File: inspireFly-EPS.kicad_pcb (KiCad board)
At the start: 4 copper layers, 88 x 94.5 mm, 123 parts, among them J1 USB4085-GF-A_REVB, J2 Conn_01x02_Pin, Q1 SQJ123ELP-T1_GE3, Q10 SQJA62EP-T1_GE3, Q3 SQJA62EP-T1_GE3, Q4 SQJA62EP-T1_GE3, Q5 SQJA62EP-T1_GE3, Q6 SQJA62EP-T1_GE3, Q7 SQJA62EP-T1_GE3, Q8 SQJA62EP-T1_GE3, Q9 SQJA62EP-T1_GE3, SW1 SW_Push, SW2 SW_Push, U1 STM32U575RIT6, U2 BQ25750RRVR, U3 TCAN332DCNR, U4 MAX77504AAFC+T, U6 INA180A3IDBVT, U8 TPS63070RNMR, U9 TPS63070RNMR, Y1 Crystal_GND2

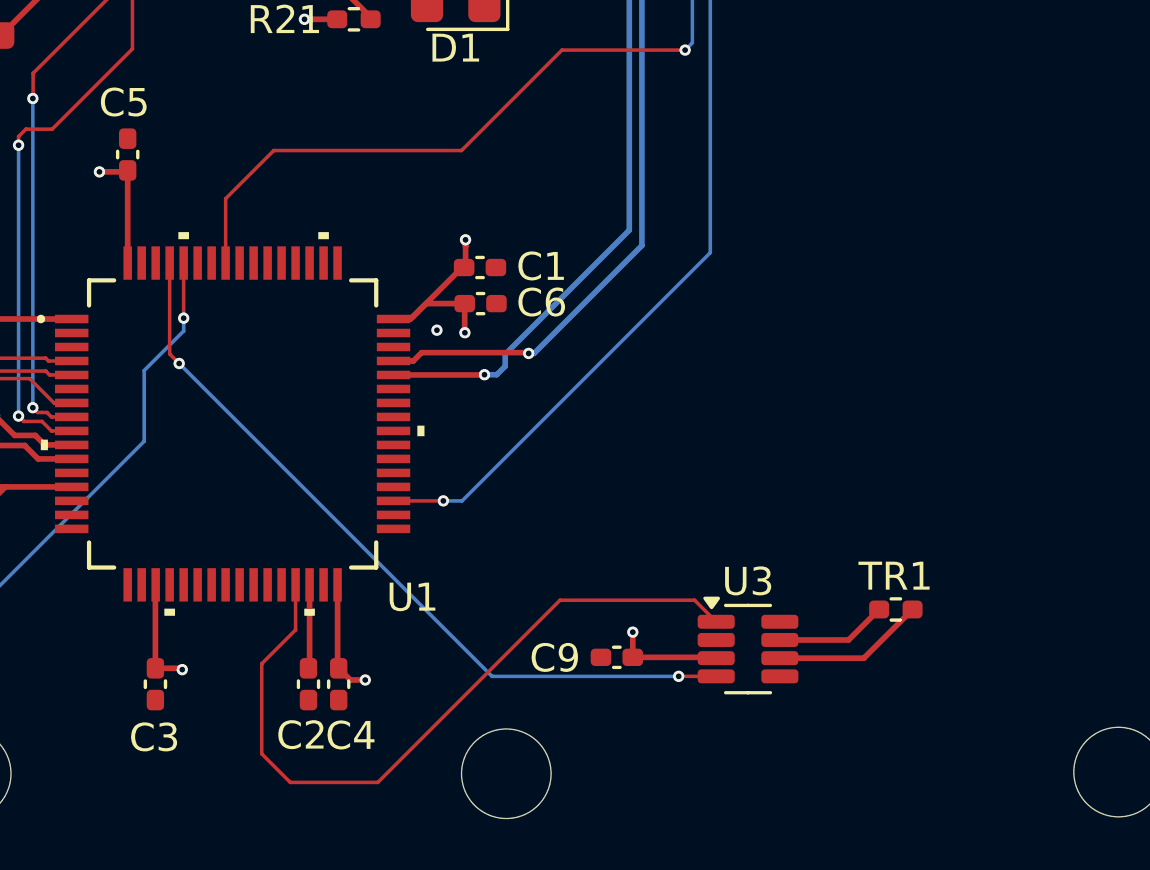
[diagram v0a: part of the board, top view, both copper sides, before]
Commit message: Updated the ST575 to have a 14 pin debugger
Routed and added to schematic.
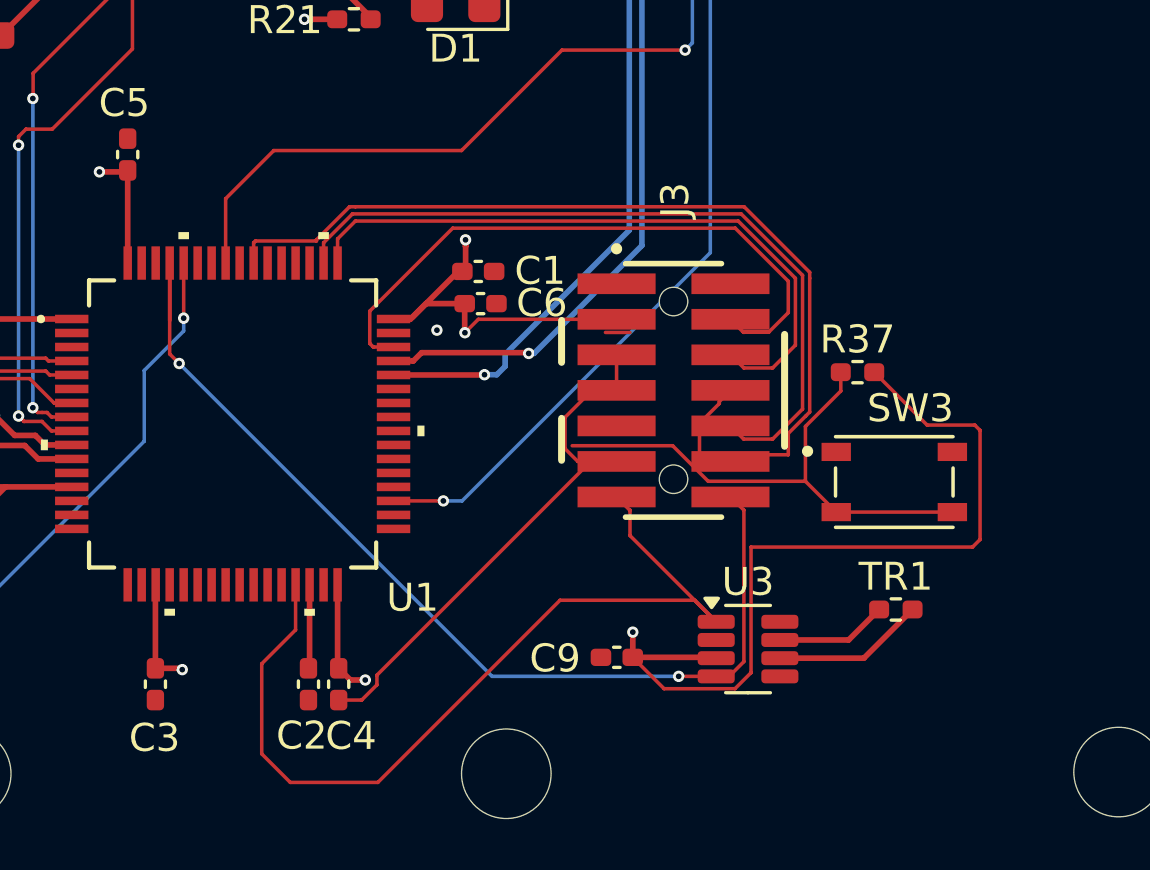
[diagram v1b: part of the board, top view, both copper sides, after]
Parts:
- added J3: FTSH-107-01-L-DV-K-A, inspireFly-EPS-footprints:SAMTEC_FTSH-107-01-L-DV-K-A, F.Cu at (77.0, 89.0)
- added R37: 10K, Resistor_SMD:R_0402_1005Metric_Pad0.72x0.64mm_HandSolder, F.Cu at (83.5, 88.3)
- added SW3: SW_Push, inspireFly-EPS-footprints:SW_PTS810_SJM_250_SMTR_LFS, F.Cu at (84.8, 92.2)
- moved C1 0.15 mm to (70.0, 84.7)
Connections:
- U1 pad 46: unconnected-(U1A-PA13-Pad46) -> JTMS/SWDIO
- U1 pad 49: unconnected-(U1A-PA14-Pad49) -> JTCK/SWCLK
- U1 pad 50: unconnected-(U1A-PA15-Pad50) -> JTDI
- U1 pad 55: unconnected-(U1A-PB3-Pad55) -> SWO
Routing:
- net SWO: track 0.00 -> 34.9 mm
- net +3.3V: track 56.8 -> 89.5 mm
- net JTDI: track 0.00 -> 27.2 mm
- net JTMS/SWDIO: track 0.00 -> 23.6 mm
- net JTCK/SWCLK: track 0.00 -> 23.6 mm
- net GND: track 52.1 -> 72.4 mm
- net NRST: track 0.00 -> 19.0 mm
- net CAN_RX: track 27.6 -> 36.9 mm
- net CAN_TX: track 26.2 -> 32.2 mm

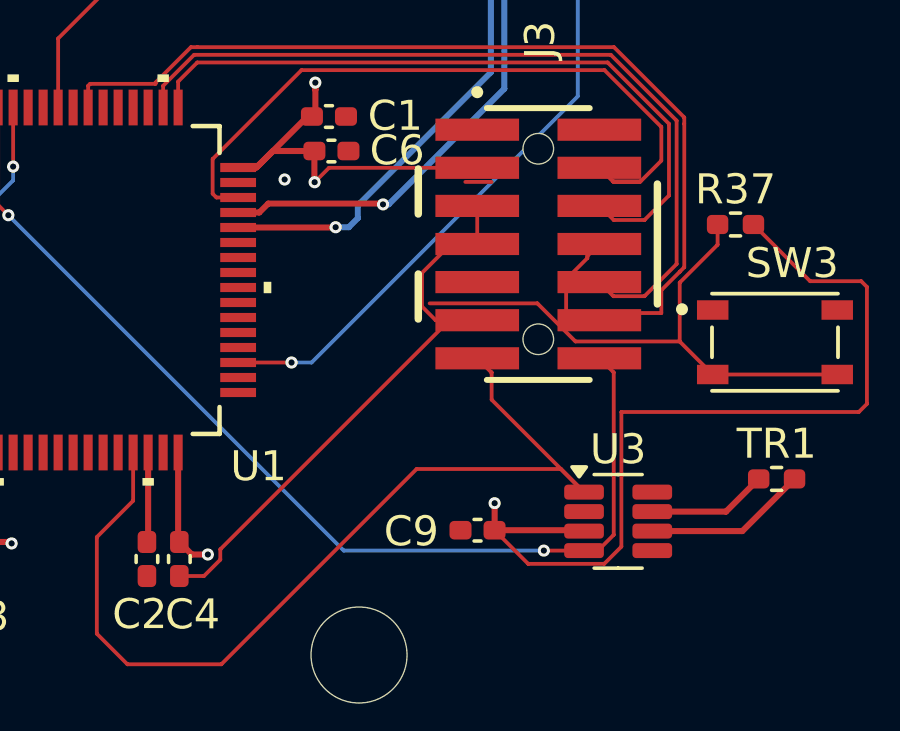
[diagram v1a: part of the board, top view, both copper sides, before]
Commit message: Routing and STLink debugger.
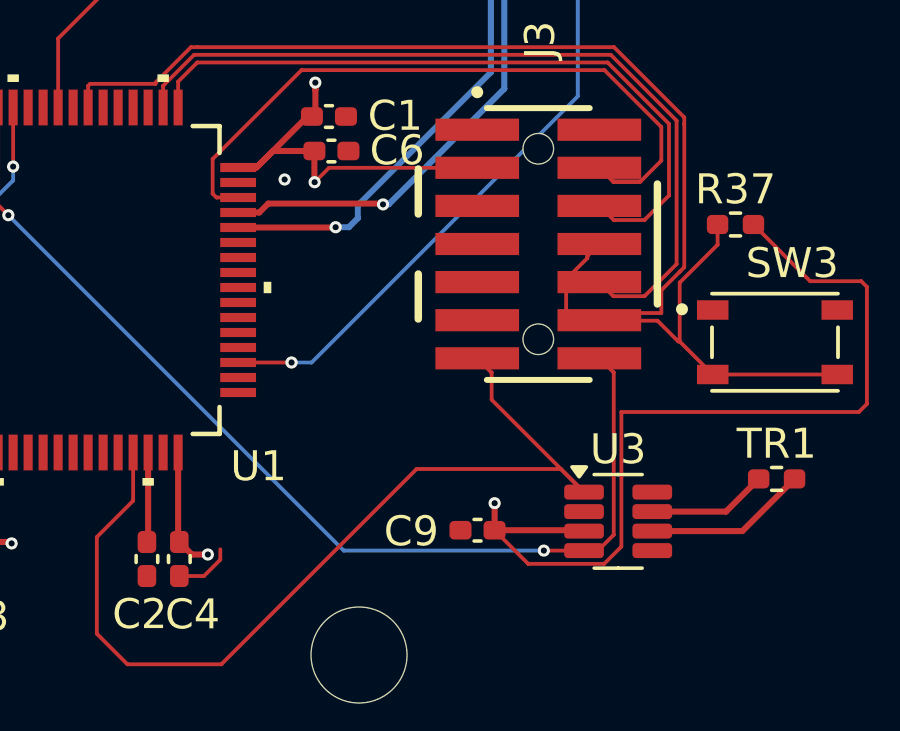
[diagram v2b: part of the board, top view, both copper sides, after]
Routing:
- net GND: track 72.4 -> 55.8 mm
- net NRST: track 19.0 -> 13.1 mm
- net +3.3V: track 89.5 -> 88.7 mm
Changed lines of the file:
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@@
 			(psa4output no)
 			(plot_black_and_white yes)
+			(plotinvisibletext no)
 			(sketchpadsonfab no)
 			(plotpadnumbers no)
@@
 	)
 	(segment
-		(start 74.522 86.88)
-		(end 75.4 86.88)
-		(width 0.127)
-		(layer "F.Cu")
-		(net 1)
-	)
-	(segment
 		(start 102.085063 51.33)
 		(end 101.405 52.010063)
@@
 	)
 	(segment
-		(start 73.534376 91.49)
-		(end 73.0785 91.034124)
-		(width 0.127)
-		(layer "F.Cu")
-		(net 125)
-	)
-	(segment
 		(start 63.749089 66.709811)
 		(end 62.9989 67.46)
@@
 	)
 	(segment
-		(start 73.0785 91.034124)
-		(end 73.0785 89.9135)
-		(width 0.127)
-		(layer "F.Cu")
-		(net 125)
-	)
-	(segment
 		(start 74.92 91.49)
 		(end 73.993745 91.49)
@@
 	)
 	(segment
-		(start 73.0785 89.9135)
-		(end 74.042 88.95)
-		(width 0.127)
-		(layer "F.Cu")
-		(net 125)
-	)
-	(segment
 		(start 88.76 55.73518)
 		(end 89.51 56.48518)
@@
 	)
 	(segment
-		(start 74.92 88.95)
-		(end 74.92 87.68)
-		(width 0.127)
-		(layer "F.Cu")
-		(net 125)
-	)
-	(segment
 		(start 89.51 56.48518)
 		(end 89.22982 56.205)
@@
 	)
 	(segment
-		(start 73.993745 91.49)
-		(end 66.3561 99.127645)
-		(width 0.127)
-		(layer "F.Cu")
-		(net 125)
-	)
-	(segment
 		(start 87.89 45.65)
 		(end 87.89 46.3875)
@@
 	)
 	(segment
-		(start 74.92 91.49)
-		(end 73.534376 91.49)
-		(width 0.127)
-		(layer "F.Cu")
-		(net 125)
-	)
-	(segment
 		(start 65.94 29.77)
 		(end 66.31 30.14)
@@
 	)
 	(segment
-		(start 78.194519 92.1985)
-		(end 81.6685 92.1985)
+		(start 82.77 93.3)
+		(end 86.92 93.3)
 		(width 0.127)
 		(layer "F.Cu")
@@
 	)
 	(segment
-		(start 82.77 93.3)
-		(end 86.92 93.3)
+		(start 81.6685 92.1985)
+		(end 81.6215 92.1985)
 		(width 0.127)
 		(layer "F.Cu")
@@
 	)
 	(segment
-		(start 76.924519 90.9285)
-		(end 78.194519 92.1985)
+		(start 81.6215 92.1985)
+		(end 80.9295 91.5065)
 		(width 0.127)
 		(layer "F.Cu")
@@
 	)
 	(segment
-		(start 73.3335 90.9285)
-		(end 76.924519 90.9285)
+		(start 80.9295 91.5065)
+		(end 78.99 91.5065)
 		(width 0.127)
 		(layer "F.Cu")

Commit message: Schematic rework
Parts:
- added H1: MountingHole_Pad, MountingHole:MountingHole_2.2mm_M2_Pad_TopBottom, F.Cu at (38.7, 124.4)
- added H2: MountingHole_Pad, MountingHole:MountingHole_2.2mm_M2_Pad_TopBottom, F.Cu at (102.7, 124.4)
- moved C21 94.0 mm to (156.3, 73.0)
- moved C35 94.0 mm to (136.3, 63.6)
- moved J2 94.0 mm to (146.8, 38.4)
- moved R3 94.0 mm to (145.6, 80.9)
- moved C11 94.0 mm to (145.4, 85.2)
- moved C24 94.0 mm to (177.6, 41.6)
- moved C26 94.0 mm to (143.2, 93.8)
- moved C27 94.0 mm to (144.4, 102.0)
- moved C30 94.0 mm to (193.9, 59.1)
- moved C37 94.0 mm to (176.4, 57.4)
- moved C38 94.0 mm to (183.4, 52.7)
- moved C39 94.0 mm to (181.5, 59.2)
- moved C4 94.0 mm to (158.3, 110.5)
- moved C42 94.0 mm to (182.8, 42.7)
- moved C45 94.0 mm to (178.4, 70.3)
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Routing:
- net SWO: track 34.9 -> 29.1 mm, vias 0 -> 2
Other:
- board size 88 x 94.5 mm -> 94 x 87 mm

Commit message: Routing Updates
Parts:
- removed C1, C18, C19: 100nF, Capacitor_SMD:C_0402_1005Metric_Pad0.74x0.62mm_HandSolder
- removed C10, C11: 100nF, Capacitor_SMD:C_0805_2012Metric_Pad1.18x1.45mm_HandSolder
- removed C12: 470nF, Capacitor_SMD:C_1206_3216Metric_Pad1.33x1.80mm_HandSolder
- removed C13, C23: 2.2uF, Capacitor_SMD:C_1206_3216Metric_Pad1.33x1.80mm_HandSolder
- removed C15, C16: 47nF, Capacitor_SMD:C_0402_1005Metric_Pad0.74x0.62mm_HandSolder
- removed C17: 47uF, inspireFly-EPS-footprints:CAP_EEEFN1J470L
- removed C20: 470nF, Capacitor_SMD:C_0402_1005Metric_Pad0.74x0.62mm_HandSolder
- removed C21, C22: 4.7uF, Capacitor_SMD:C_0402_1005Metric_Pad0.74x0.62mm_HandSolder
- removed C35, C36, C50: 22uF, Capacitor_SMD:C_0805_2012Metric_Pad1.18x1.45mm_HandSolder
- removed C51: 10pF, Capacitor_SMD:C_0402_1005Metric_Pad0.74x0.62mm_HandSolder
- removed D1: LED, Diode_SMD:D_0805_2012Metric_Pad1.15x1.40mm_HandSolder
- removed D4, D5: DFLS130L-7, inspireFly-EPS-footprints:DFLS130L7
- removed G***: LOGO, inspireFly-EPS-footprints:inspireFly_Logo_long
- removed J1: USB4085-GF-A_REVB, inspireFly-EPS-footprints:GCT_USB4085-GF-A_REVB
- removed JP1: BAT_ENABLE, Jumper:SolderJumper-2_P1.3mm_Open_RoundedPad1.0x1.5mm
- removed L1: 2.2uH, inspireFly-EPS-footprints:WE-MXGI_4020
- removed Q1: SQJ123ELP-T1_GE3, inspireFly-EPS-footprints:TRANS_SQJA62EP-T1_GE3
- removed Q10, Q3, Q4, Q5, Q6, Q7, Q8, Q9: SQJA62EP-T1_GE3, inspireFly-EPS-footprints:TRANS_SQJA62EP-T1_GE3
- removed R1, R5: 5m, Resistor_SMD:R_1206_3216Metric_Pad1.30x1.75mm_HandSolder
- removed R12: 40k, Resistor_SMD:R_0402_1005Metric_Pad0.72x0.64mm_HandSolder
- removed R13: 3.3k, Resistor_SMD:R_0402_1005Metric_Pad0.72x0.64mm_HandSolder
- removed R14: 12.5k, Resistor_SMD:R_0402_1005Metric_Pad0.72x0.64mm_HandSolder
- removed R15: 47k, Resistor_SMD:R_0603_1608Metric_Pad0.98x0.95mm_HandSolder
- removed R18, R19: 10k, Resistor_SMD:R_0402_1005Metric_Pad0.72x0.64mm_HandSolder
- removed R2, R3, R6, R7: 10, Resistor_SMD:R_0603_1608Metric_Pad0.98x0.95mm_HandSolder
- removed R20: 330, Resistor_SMD:R_0402_1005Metric_Pad0.72x0.64mm_HandSolder
- removed R21, R33, R34, R35, R36: 10K, Resistor_SMD:R_0402_1005Metric_Pad0.72x0.64mm_HandSolder
- removed R4: 2, Resistor_SMD:R_1206_3216Metric_Pad1.30x1.75mm_HandSolder
- removed R8: 200k, Resistor_SMD:R_0402_1005Metric_Pad0.72x0.64mm_HandSolder
- removed R9: 44.8k, Resistor_SMD:R_0402_1005Metric_Pad0.72x0.64mm_HandSolder
- removed SW1, SW2: SW_Push, inspireFly-EPS-footprints:SW_PTS810_SJM_250_SMTR_LFS
- removed TP1: DRV_SUP, TestPoint:TestPoint_Pad_D1.5mm
- removed TP2: V_PROTECTED, TestPoint:TestPoint_Pad_D1.5mm
- removed TP5: V_BAT, TestPoint:TestPoint_Pad_D1.5mm
- removed U1: STM32U575RIT6, inspireFly-EPS-footprints:LQFP64-10x10mm_STM
- removed U2: BQ25750RRVR, inspireFly-EPS-footprints:VQFN36_RRV_TEX
- removed Y1: Crystal_GND2, inspireFly-EPS-footprints:XTAL_TSX-3225_16.0000MF18X-AC0
- added C53: 100nF, Capacitor_SMD:C_0402_1005Metric_Pad0.74x0.62mm_HandSolder, F.Cu at (70.3, 60.6)
- added C54: 470nF, Capacitor_SMD:C_0402_1005Metric_Pad0.74x0.62mm_HandSolder, F.Cu at (71.7, 59.3)
- added C55: 100nF, Capacitor_SMD:C_0402_1005Metric_Pad0.74x0.62mm_HandSolder, F.Cu at (69.8, 58.6)
- added C57: 4.7uF, Capacitor_SMD:C_0402_1005Metric_Pad0.74x0.62mm_HandSolder, F.Cu at (77.6, 55.4)
- added C58: 4.7uF, Capacitor_SMD:C_0402_1005Metric_Pad0.74x0.62mm_HandSolder, F.Cu at (74.9, 55.3)
- added C59: 1uF, Capacitor_SMD:C_0402_1005Metric_Pad0.74x0.62mm_HandSolder, F.Cu at (69.3, 63.9)
- added C61: 100nF, Capacitor_SMD:C_0402_1005Metric_Pad0.74x0.62mm_HandSolder, F.Cu at (73.4, 55.4)
- added C62: 100nF, Capacitor_SMD:C_0402_1005Metric_Pad0.74x0.62mm_HandSolder, F.Cu at (79.9, 55.3)
- added C63: 100nF, Capacitor_SMD:C_0402_1005Metric_Pad0.74x0.62mm_HandSolder, F.Cu at (84.1, 58.5)
- added C64: 470nF, Capacitor_SMD:C_0402_1005Metric_Pad0.74x0.62mm_HandSolder, F.Cu at (81.0, 60.0)
- added C65: 100nF, Capacitor_SMD:C_0402_1005Metric_Pad0.74x0.62mm_HandSolder, F.Cu at (84.1, 59.6)
- added C66: 10nF, Capacitor_SMD:C_0402_1005Metric_Pad0.74x0.62mm_HandSolder, F.Cu at (40.1, 48.9)
- added C68: 10nF, Capacitor_SMD:C_0402_1005Metric_Pad0.74x0.62mm_HandSolder, F.Cu at (35.7, 48.9)
- added C69: 22uF, Capacitor_SMD:C_0805_2012Metric_Pad1.18x1.45mm_HandSolder, F.Cu at (30.9, 50.4)
- added C70: 22uF, Capacitor_SMD:C_0805_2012Metric_Pad1.18x1.45mm_HandSolder, F.Cu at (30.9, 48.1)
- added C71: 22uF, Capacitor_SMD:C_0805_2012Metric_Pad1.18x1.45mm_HandSolder, F.Cu at (62.1, 79.5)
- added C72: 22uF, Capacitor_SMD:C_0805_2012Metric_Pad1.18x1.45mm_HandSolder, F.Cu at (62.1, 81.9)
- added C73: 22uF, Capacitor_SMD:C_0805_2012Metric_Pad1.18x1.45mm_HandSolder, F.Cu at (62.1, 74.8)
- added C74: 22uF, Capacitor_SMD:C_0805_2012Metric_Pad1.18x1.45mm_HandSolder, F.Cu at (62.1, 77.0)
- added C75: 22uF, Capacitor_SMD:C_0805_2012Metric_Pad1.18x1.45mm_HandSolder, F.Cu at (47.1, 53.8)
- added C76: 22uF, Capacitor_SMD:C_0805_2012Metric_Pad1.18x1.45mm_HandSolder, F.Cu at (47.1, 50.4)
- added C77: 22uF, Capacitor_SMD:C_0805_2012Metric_Pad1.18x1.45mm_HandSolder, F.Cu at (48.3, 46.2)
- added C78: 22uF, Capacitor_SMD:C_0805_2012Metric_Pad1.18x1.45mm_HandSolder, F.Cu at (45.1, 46.2)
- added C79: 22uF, Capacitor_SMD:C_0805_2012Metric_Pad1.18x1.45mm_HandSolder, F.Cu at (30.9, 45.9)
- added C80: 22uF, Capacitor_SMD:C_0805_2012Metric_Pad1.18x1.45mm_HandSolder, F.Cu at (58.8, 57.0)
- added D3: LTST-S270KRKT, LED_SMD:LED_0603_1608Metric_Pad1.05x0.95mm_HandSolder, F.Cu at (78.0, 67.3)
- added J5: USB4110-GF-A, inspireFly-EPS-footprints:USB4110-GF-A_GCT, F.Cu at (71.4, 45.0)
- added JP2: FTSW EN, Jumper:SolderJumper-2_P1.3mm_Open_TrianglePad1.0x1.5mm, F.Cu at (28.5, 43.1)
- added L5: 10uH, inspireFly-EPS-footprints:WE-XHMA_1090, F.Cu at (49.5, 64.3)
- added Q14: SQJA62EP-T1_GE3, inspireFly-EPS-footprints:TRANS_SQJA62EP-T1_GE3, F.Cu at (61.1, 70.0)
- added Q15: SQJA62EP-T1_GE3, inspireFly-EPS-footprints:TRANS_SQJA62EP-T1_GE3, F.Cu at (52.7, 74.3)
- added Q16: SQJA62EP-T1_GE3, inspireFly-EPS-footprints:TRANS_SQJA62EP-T1_GE3, F.Cu at (53.2, 54.0)
- added Q17: SQJA62EP-T1_GE3, inspireFly-EPS-footprints:TRANS_SQJA62EP-T1_GE3, F.Cu at (61.1, 62.1)
- added R10: 390k, Resistor_SMD:R_0402_1005Metric, F.Cu at (35.4, 42.4)
- added R11: 110k, Resistor_SMD:R_0402_1005Metric, F.Cu at (33.0, 42.4)
- added R17: 47k, Resistor_SMD:R_0402_1005Metric_Pad0.72x0.64mm_HandSolder, F.Cu at (81.6, 62.9)
- added R38: 210k, Resistor_SMD:R_0402_1005Metric_Pad0.72x0.64mm_HandSolder, F.Cu at (81.6, 61.7)
- added R39: 10, Resistor_SMD:R_0402_1005Metric_Pad0.72x0.64mm_HandSolder, F.Cu at (68.3, 60.8)
- added R40: 6.2k, Resistor_SMD:R_0402_1005Metric_Pad0.72x0.64mm_HandSolder, F.Cu at (81.6, 65.3)
- added R41: 36k, Resistor_SMD:R_0402_1005Metric_Pad0.72x0.64mm_HandSolder, F.Cu at (81.6, 66.4)
- added R42: 5m, Resistor_SMD:R_1206_3216Metric_Pad1.30x1.75mm_HandSolder, F.Cu at (58.3, 77.7)
- added R43: 15k, Resistor_SMD:R_0402_1005Metric_Pad0.72x0.64mm_HandSolder, F.Cu at (81.6, 64.2)
- added R44: 40k, Resistor_SMD:R_0402_1005Metric_Pad0.72x0.64mm_HandSolder, F.Cu at (71.5, 63.2)
- added R45: 10, Resistor_SMD:R_0402_1005Metric_Pad0.72x0.64mm_HandSolder, F.Cu at (66.1, 60.8)
- added R46: 10k, Resistor_SMD:R_0402_1005Metric_Pad0.72x0.64mm_HandSolder, F.Cu at (75.3, 65.2)
- added R47: 10k, Resistor_SMD:R_0402_1005Metric_Pad0.72x0.64mm_HandSolder, F.Cu at (77.6, 65.2)
- added R48: 10, Resistor_SMD:R_0402_1005Metric_Pad0.72x0.64mm_HandSolder, F.Cu at (76.2, 55.4)
- added R49: 10, Resistor_SMD:R_0402_1005Metric_Pad0.72x0.64mm_HandSolder, F.Cu at (84.1, 57.3)
- added R50: 5m, Resistor_SMD:R_1206_3216Metric_Pad1.30x1.75mm_HandSolder, F.Cu at (52.4, 46.4)
- added R51: 10, Resistor_SMD:R_0402_1005Metric_Pad0.72x0.64mm_HandSolder, F.Cu at (84.1, 60.6)
- added R52: 680, Resistor_SMD:R_0402_1005Metric_Pad0.72x0.64mm_HandSolder, F.Cu at (37.9, 48.9)
- added R53: 390k, Resistor_SMD:R_0402_1005Metric, F.Cu at (35.5, 43.7)
- added R54: 100k, Resistor_SMD:R_0402_1005Metric_Pad0.72x0.64mm_HandSolder, F.Cu at (138.1, 69.8)
- added RN1: YC158TJR-072K2L, inspireFly-EPS-footprints:RESCAXE64P320X160X70-10N, F.Cu at (141.3, 50.4)
- added SW4: SW_TL1015AF160QG, inspireFly-EPS-footprints:SW_TL1015AF160QG, F.Cu at (134.3, 79.0)
- added U10: BQ25756ERRVR, inspireFly-EPS-footprints:IC_BQ25756ERRVR, F.Cu at (76.5, 60.6)
- added U13: TPS259472ARPWR, inspireFly-EPS-footprints:RPW0010A-MFG, F.Cu at (36.7, 46.0)
- added U5: STM32U575CIT6, inspireFly-EPS-footprints:LQFP48-7x7mm_STM, F.Cu at (156.2, 52.5)
- added Y2: XTAL_ABS07-32.768KHZ-T, inspireFly-EPS-footprints:XTAL_ABS07-32.768KHZ-T, F.Cu at (171.9, 54.3)
- C25: value 100nF -> 22pF
- C26: value 10pF -> 22pF
- C6: value 10uF -> 1uF
- R37: value 10K -> 10k
- SW3: value SW_Push -> SW_TL1015AF160QG; footprint inspireFly-EPS-footprints:SW_PTS810_SJM_250_SMTR_LFS -> inspireFly-EPS-footprints:SW_TL1015AF160QG
- moved C40 229.8 mm to (-20.9, 106.4), turned to 0 degrees
- moved C34 224.8 mm to (-20.9, 97.3), turned to 0 degrees
- moved C31 223.1 mm to (-20.9, 94.3), turned to 0 degrees
- moved TP4 222.6 mm to (-14.3, 84.9)
- moved C44 218.4 mm to (-22.5, 124.5)
- moved C46 217.5 mm to (-21.6, 141.0), turned to 0 degrees
- moved C30 217.2 mm to (-20.9, 91.3)
- moved C49 216.7 mm to (-22.5, 136.5), turned to 0 degrees
- moved TP7 213.8 mm to (-15.9, 125.0)
- moved C48 213.1 mm to (-22.5, 133.5), turned to 0 degrees
- moved R27 212.8 mm to (-12.8, 98.5), turned to 0 degrees
- moved U4 212.8 mm to (-15.5, 102.4)
- moved R26 212.7 mm to (-12.8, 96.5)
- moved C47 209.4 mm to (-22.5, 130.5), turned to 0 degrees
- moved C45 208.9 mm to (-22.5, 127.5), turned to 0 degrees
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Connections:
- net BAT + renamed BAT+
- net V_BUS_COMBINED renamed EXTERNAL_VOLTAGE
- net V_PROTECTED renamed PROTECTED_VOLTAGE
- C25 pad 1: Net-(U1A-NRST) -> GND
- J3 pad 13: CAN_TX -> DEBUG_LPUART_TX
- J3 pad 14: CAN_RX -> DEBUG_LPUART_RX
- R37 pad 1: NRST -> +3.3V
- R37 pad 2: +3.3V -> NRST
- SW3 pad 1: GND -> NRST
- SW3 pad 2: NRST -> GND
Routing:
- net Net-(U6-OUT): track 93.7 -> 0.00 mm, vias 4 -> 0
- net +3.3V: track 88.7 -> 0.00 mm, vias 20 -> 0
- net USB_CC2: track 84.8 -> 0.00 mm, vias 1 -> 0
- net USB_CC1: track 78.1 -> 0.00 mm, vias 1 -> 0
- net USB_D+: track 75.0 -> 0.00 mm, vias 1 -> 0
- net USB_D-: track 74.6 -> 0.00 mm, vias 1 -> 0
- net EXTERNAL_VOLTAGE: track 84.6 -> 20.1 mm, vias 2 -> 13
- net Net-(Q4-D): track 61.6 -> 0.00 mm, vias 2 -> 0
- net Net-(BT1-Pad1-): track 60.4 -> 0.00 mm
- net Net-(Q1-D): track 58.4 -> 0.00 mm, vias 2 -> 0
- net Net-(Q3-G): track 51.7 -> 0.00 mm, vias 2 -> 0
- net EXTERNAL_SIDE_INDUC: track 0.00 -> 50.0 mm, vias 0 -> 2
- net PROTECTED_VOLTAGE: track 48.6 -> 0.00 mm, vias 2 -> 0
- net EXTERNAL_HIGH_SIDE_DRIVE: track 0.00 -> 47.6 mm, vias 0 -> 2
- net GND: track 55.8 -> 13.0 mm
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- added copper zone on F.Cu, net BAT_SIDE_INDUC
- added copper zone on F.Cu, net EXTERNAL_SIDE_INDUC
- added copper zone on In2.Cu, net EXTERNAL_VOLTAGE
- added copper zone on B.Cu, net Net-(BT1-Pad1-)
- added copper zone on F.Cu, net Net-(Q14-D)
- added copper zone on F.Cu, net Net-(Q16-D)
- removed copper zone on F.Cu, net +3.3V
- removed copper zone on In2.Cu, net +3.3V
- removed copper zone on F.Cu, net +5V
- removed copper zone on In2.Cu, net +5V
- removed copper zone on F.Cu, net +9V
- removed copper zone on F.Cu, net Net-(Q1-D)
- removed copper zone on F.Cu, net Net-(Q10-D)
- removed copper zone on F.Cu, net Net-(Q10-S)
- removed copper zone on F.Cu, net Net-(Q3-S)
- removed copper zone on F.Cu, net Net-(Q4-D)
- removed copper zone on F.Cu, net Net-(Q5-S)
- removed copper zone on F.Cu, net Net-(Q7-S)
- removed copper zone on F.Cu, net Net-(U4-LX)
- removed copper zone on F.Cu, net Net-(U6-IN+)
- removed copper zone on F.Cu, net PROTECTED_VOLTAGE
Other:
- board text removed: "+3.3V"
- board text removed: "+5V"
- board text removed: "+9V"
- board text removed: "BAT+"
- board text removed: "BOOT"
- board text removed: "DRV_SUP"
- board text removed: "Design by inspireFly Avionics Memebers"
- board text removed: "GND"
- board text removed: "RESET"
- board text removed: "V_BAT"
- board text removed: "V_COMBINED"
- board text removed: "V_PROTECTED"
- board text removed: "inspireFly EPS Main Board Rev A.1 Proto"

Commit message: 3.3V routing changes
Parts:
- removed C34, C41: 22uF, Capacitor_SMD:C_0805_2012Metric_Pad1.18x1.45mm_HandSolder
- added J4: Conn_01x02_Pin, Connector_PinSocket_2.54mm:PinSocket_1x02_P2.54mm_Vertical, F.Cu at (152.7, 84.7)
- C30, C37, C38, C44, C45: footprint Capacitor_SMD:C_0805_2012Metric_Pad1.18x1.45mm_HandSolder -> Capacitor_SMD:C_0402_1005Metric_Pad0.74x0.62mm_HandSolder
- moved C27 199.8 mm to (175.5, 45.0)
- moved R22 166.6 mm to (172.3, 45.0)
- moved J3 73.8 mm to (95.7, 46.4), turned to 90 degrees
- moved C40 70.2 mm to (42.9, 76.9), turned to 90 degrees
- moved C38 68.6 mm to (44.1, 56.5)
- moved C31 68.4 mm to (45.3, 76.9), turned to 90 degrees
- moved C24 61.3 mm to (39.2, 67.2)
- moved TP4 60.0 mm to (44.3, 72.6)
- moved C43 57.7 mm to (36.0, 64.6), turned to 90 degrees
- moved C37 57.5 mm to (33.0, 56.0), turned to 90 degrees
- moved U5 57.2 mm to (99.8, 62.0)
- moved C39 56.4 mm to (37.2, 60.2)
- moved C30 56.2 mm to (32.2, 73.0), turned to 180 degrees
- moved U4 56.1 mm to (34.1, 76.3)
- moved C42 55.8 mm to (33.1, 64.6), turned to 90 degrees
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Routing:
- net Net-(U8-FB): track 0.00 -> 11.1 mm, vias 0 -> 2
- net Net-(U6-IN+): track 0.00 -> 9.44 mm
- net +3.3V: track 0.00 -> 6.32 mm, vias 0 -> 7
- net Net-(U4-LX): track 0.00 -> 5.48 mm, vias 0 -> 2
- net Net-(U4-FB): track 0.00 -> 3.89 mm
- net PROTECTED_VOLTAGE: track 0.00 -> 2.60 mm
- net Net-(U4-BST): track 0.00 -> 2.08 mm
- net Net-(U4-SEL): track 0.00 -> 2.00 mm
- net +5V: track 0.00 -> 1.98 mm, vias 0 -> 6
- net Net-(U4-VL): track 0.00 -> 1.65 mm
- net Net-(U8-VAUX): track 0.00 -> 1.31 mm
- net GND: vias 9 -> 14
- added copper zone on F.Cu, net +3.3V
- added copper zone on In2.Cu, net +3.3V
- added copper zone on F.Cu, net +5V
- added copper zone on In2.Cu, net Net-(BT1-Pad1-)
- added copper zone on F.Cu, net Net-(U4-LX)
- added copper zone on F.Cu, net Net-(U6-IN+)
- added copper zone on F.Cu, net Net-(U8-L1)
- added copper zone on F.Cu, net Net-(U8-L2)
- removed copper zone on B.Cu, net Net-(BT1-Pad1-)

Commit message: Pushing routing changes, finailize vreg locations
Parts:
- moved C47 75.9 mm to (50.4, 91.4), turned to 90 degrees
- moved C49 72.9 mm to (48.0, 91.4), turned to 90 degrees
- moved C48 70.9 mm to (45.7, 91.4), turned to 90 degrees
- moved C45 68.4 mm to (42.4, 90.7), turned to -90 degrees
- moved TP7 67.5 mm to (48.3, 86.8)
- moved C46 62.7 mm to (38.8, 92.9), turned to -90 degrees
- moved C44 61.6 mm to (35.2, 88.3), turned to 90 degrees
- moved R30 57.9 mm to (43.1, 85.4)
- moved U9 56.7 mm to (38.5, 89.8), turned to 90 degrees
- moved R31 55.9 mm to (43.1, 86.6)
- moved R32 55.7 mm to (43.2, 87.7)
- moved L4 48.0 mm to (38.8, 85.0)
- moved C29 21.1 mm to (13.8, 91.5)
- moved R24 21.1 mm to (14.8, 97.4)
- moved C69 1.08 mm to (28.6, 51.5)
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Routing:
- net Net-(U9-FB): track 0.00 -> 9.16 mm, vias 0 -> 2
- net +9V: track 0.00 -> 2.79 mm, vias 0 -> 4
- net PROTECTED_VOLTAGE: track 2.60 -> 4.07 mm
- net Net-(U9-VAUX): track 0.00 -> 1.41 mm
- net Net-(R31-Pad1): track 0.00 -> 1.13 mm
- net GND: vias 14 -> 16
- added copper zone on F.Cu, net +9V
- added copper zone on F.Cu, net Net-(U9-L1)
- added copper zone on F.Cu, net Net-(U9-L2)
- added copper zone on F.Cu, net PROTECTED_VOLTAGE

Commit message: Finished Linear Charger Schematic
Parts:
- added C34: 1uF, Capacitor_SMD:C_0402_1005Metric_Pad0.74x0.62mm_HandSolder, F.Cu at (85.0, 75.0)
- added C41: 1uF, Capacitor_SMD:C_0402_1005Metric_Pad0.74x0.62mm_HandSolder, F.Cu at (110.1, 76.0)
- added C51: 1.5F, inspireFly-EPS-footprints:CH3R6155CF-ZJN, F.Cu at (101.0, 94.5)
- added C52: 1.5F, inspireFly-EPS-footprints:CH3R6155CF-ZJN, F.Cu at (78.5, 94.5)
- added R35: 604, Resistor_SMD:R_0402_1005Metric_Pad0.72x0.64mm_HandSolder, F.Cu at (89.6, 75.0)
- added R36: 100k, Resistor_SMD:R_0402_1005Metric_Pad0.72x0.64mm_HandSolder, F.Cu at (89.6, 78.0)
- added R55: 806k, Resistor_SMD:R_0402_1005Metric_Pad0.72x0.64mm_HandSolder, F.Cu at (99.1, 81.0)
- added R56: 10k, Resistor_SMD:R_0402_1005Metric_Pad0.72x0.64mm_HandSolder, F.Cu at (105.6, 76.0)
- added R57: 10k, Resistor_SMD:R_0402_1005Metric_Pad0.72x0.64mm_HandSolder, F.Cu at (105.4, 79.0)
- added U1: BQ25173DSGR, inspireFly-EPS-footprints:DSG0008A-IPC_B, F.Cu at (99.0, 75.7)
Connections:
- C14 pad 1: +3.3V -> BQ2_STAT
- C24 pad 1: +3.3V -> BQ2_STAT
- C3 pad 1: +3.3V -> BQ2_STAT
- C31 pad 2: +3.3V -> BQ2_STAT
- C4 pad 1: +3.3V -> BQ2_STAT
- C40 pad 2: +3.3V -> BQ2_STAT
- C5 pad 1: +3.3V -> BQ2_STAT
- C6 pad 1: +3.3V -> BQ2_STAT
- C7 pad 1: +3.3V -> BQ2_STAT
- C8 pad 1: +3.3V -> BQ2_STAT
- C9 pad 1: +3.3V -> BQ2_STAT
- J3 pad 03: +3.3V -> BQ2_STAT
- L2 pad 2: +3.3V -> BQ2_STAT
- R26 pad 2: +3.3V -> BQ2_STAT
- R37 pad 1: +3.3V -> BQ2_STAT
- R46 pad 2: +3.3V -> BQ2_STAT
- RN1 pad 10: +3.3V -> BQ2_STAT
- RN1 pad 5: +3.3V -> BQ2_STAT
- SW4 pad 2: +3.3V -> BQ2_STAT
- TP4 pad 1: +3.3V -> BQ2_STAT
- U3 pad 3: +3.3V -> BQ2_STAT
- U4 pad 9: +3.3V -> BQ2_STAT
- U5 pad 1: +3.3V -> BQ2_STAT
- U5 pad 15: unconnected-(U5-PA5-Pad15) -> BQ2_CE
- U5 pad 24: +3.3V -> BQ2_STAT
- U5 pad 29: unconnected-(U5-PA8-Pad29) -> BQ2_STAT
- U5 pad 36: +3.3V -> BQ2_STAT
- U5 pad 48: +3.3V -> BQ2_STAT
- U5 pad 9: +3.3V -> BQ2_STAT
- U6 pad 5: +3.3V -> BQ2_STAT
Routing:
- net BQ2_STAT: track 0.00 -> 6.32 mm, vias 0 -> 7
- net +3.3V: track 6.32 -> 0.00 mm, vias 7 -> 0
- added copper zone on F.Cu, net BQ2_STAT
- added copper zone on In2.Cu, net BQ2_STAT
- removed copper zone on F.Cu, net +3.3V
- removed copper zone on In2.Cu, net +3.3V
